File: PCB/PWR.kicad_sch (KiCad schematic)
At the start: 21 parts, among them U3 LT8610

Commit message: Fixed UART, cleaned schematic, improved LDO
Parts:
- C10, C11, C12, C13, C14, C15, C8, C9: footprint (none) -> Capacitor_SMD:C_0201_0603Metric_Pad0.64x0.40mm_HandSolder
- F2: footprint RF1180000 -> (none)
- R10, R12, R18, R7, R8, R9: footprint (none) -> Resistor_SMD:R_0603_1608Metric_Pad0.98x0.95mm_HandSolder
- renumbered PMOS to PMOS1, TVS to TVS1
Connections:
- net 3v3 renamed +3V3
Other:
- moved on the sheet: C15, LED1, R12, R7

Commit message: PCB layout v1.0
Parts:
- C10, C11, C12, C13, C14, C15, C8: footprint Capacitor_SMD:C_0201_0603Metric_Pad0.64x0.40mm_HandSolder -> Capacitor_SMD:C_0603_1608Metric_Pad1.08x0.95mm_HandSolder
- C9: footprint Capacitor_SMD:C_0201_0603Metric_Pad0.64x0.40mm_HandSolder -> Capacitor_SMD:C_0805_2012Metric_Pad1.18x1.45mm_HandSolder
- D3: value 9v zener -> BZX84B9V1; footprint (none) -> Package_TO_SOT_SMD:SOT-23
- F2: footprint (none) -> VNfootprints:polyfuse
- L2: value SPM3012T-4R7M-LR -> SPM3012T-1R5M-LR; footprint (none) -> VNfootprints:SPM3010-3020
- LED1: value Red -> LTST-C170KRKT
- PMOS1: value IRF4905 -> IRF4905STRLPBF; footprint (none) -> Package_TO_SOT_SMD:TO-263-2
- R12: value R -> 160
- TVS0: renamed from TVS1; value PTVS5V0Z1USK -> TSM24ADBZR; footprint Diode_SMD:Nexperia_DSN1608-2_1.6x0.8mm -> Package_TO_SOT_SMD:TSOT-23
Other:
- note removed: "powered via usb for flashing or only via power source? power source, no point to have separate ldo that turns on only when 24v not present and 5v present"
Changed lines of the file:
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@@
 		)
 	)
-	(text "powered via usb for flashing or only via power source?\n\npower source, no point to have separate ldo \nthat turns on only when 24v not present and 5v present\n"
-		(exclude_from_sim no)
-		(at 49.53 82.042 0)
-		(effects
-			(font
-				(size 1.27 1.27)
-			)
-		)
-	)
 	(junction
 		(at 158.75 55.88)
@@
 	)
 	(junction
+		(at 43.18 39.37)
+		(diameter 0)
+		(color 0 0 0 0)
+	)
+	(junction
 		(at 222.25 63.5)
 		(diameter 0)
@@
 	(wire
 		(pts
-			(xy 25.4 46.99) (xy 25.4 44.45)
+			(xy 146.05 76.2) (xy 146.05 73.66)
 		)
 		(stroke
@@
 	(wire
 		(pts
-			(xy 146.05 76.2) (xy 146.05 73.66)
+			(xy 25.4 44.45) (xy 26.67 44.45)
 		)
 		(stroke
@@
 	(wire
 		(pts
-			(xy 25.4 44.45) (xy 26.67 44.45)
+			(xy 177.8 63.5) (xy 175.26 63.5)
 		)
 		(stroke
@@
 	(wire
 		(pts
-			(xy 177.8 63.5) (xy 175.26 63.5)
+			(xy 166.37 60.96) (xy 167.64 60.96)
 		)
 		(stroke
@@
 	(wire
 		(pts
-			(xy 166.37 60.96) (xy 167.64 60.96)
+			(xy 222.25 58.42) (xy 222.25 63.5)
 		)
 		(stroke
@@
 	(wire
 		(pts
-			(xy 222.25 58.42) (xy 222.25 63.5)
+			(xy 228.6 45.72) (xy 228.6 48.26)
 		)
 		(stroke
@@
 	(wire
 		(pts
-			(xy 228.6 45.72) (xy 228.6 48.26)
+			(xy 25.4 44.45) (xy 25.4 39.37)
 		)
 		(stroke
@@
 	(wire
 		(pts
+			(xy 25.4 39.37) (xy 43.18 39.37)
+		)
+		(stroke
+			(width 0)
+			(type default)
+		)
+	)
+	(wire
+		(pts
 			(xy 177.8 60.96) (xy 175.26 60.96)
 		)
@@
 	(global_label "24Vin"
 		(shape input)
-		(at 25.4 46.99 270)
-		(fields_autoplaced yes)
-		(effects
-			(font
-				(size 1.27 1.27)
-			)
-			(justify right)
-		)
-		(property "Intersheetrefs" "${INTERSHEET_REFS}"
-			(at 25.4 55.2366 90)
-			(effects
-				(font
-					(size 1.27 1.27)
-				)
-				(justify right)
-				(hide yes)
-			)
-		)
-	)
-	(global_label "24Vin"
-		(shape input)
 		(at 43.18 38.1 90)
 		(fields_autoplaced yes)
@@
 		(dnp no)
 		(property "Reference" "C15"
-			(at 159.766 65.786 0)
+			(at 160.02 61.214 0)
 			(effects
 				(font
@@
 		)
 		(property "Value" "470n"
-			(at 160.528 61.468 0)
+			(at 160.782 65.786 0)
 			(effects
 				(font
@@
 			)
 		)
-		(property "Footprint" "Capacitor_SMD:C_0201_0603Metric_Pad0.64x0.40mm_HandSolder"
+		(property "Footprint" "Capacitor_SMD:C_0603_1608Metric_Pad1.08x0.95mm_HandSolder"
 			(at 153.9748 59.69 0)
 			(effects
@@
 		)
 		(property "Value" "GND"
-			(at 178.562 57.404 90)
+			(at 179.07 57.404 90)
 			(effects
 				(font
@@
 			)
 		)
-		(property "Footprint" ""
+		(property "Footprint" "VNfootprints:polyfuse"
 			(at 57.15 148.26 0)
 			(effects
@@
 			)
 		)
-		(property "Footprint" "Capacitor_SMD:C_0201_0603Metric_Pad0.64x0.40mm_HandSolder"
+		(property "Footprint" "Capacitor_SMD:C_0603_1608Metric_Pad1.08x0.95mm_HandSolder"
 			(at 175.26 59.9948 0)
 			(effects
@@
 		(dnp no)
 		(property "Reference" "C11"
-			(at 208.28 52.324 90)
+			(at 209.296 50.8 90)
 			(effects
 				(font
@@
 			)
 		)
-		(property "Footprint" "Capacitor_SMD:C_0201_0603Metric_Pad0.64x0.40mm_HandSolder"
+		(property "Footprint" "Capacitor_SMD:C_0603_1608Metric_Pad1.08x0.95mm_HandSolder"
 			(at 212.09 57.4548 0)
 			(effects
@@
 			)
 		)
-		(property "Footprint" "Capacitor_SMD:C_0201_0603Metric_Pad0.64x0.40mm_HandSolder"
+		(property "Footprint" "Capacitor_SMD:C_0805_2012Metric_Pad1.18x1.45mm_HandSolder"
 			(at 177.4952 46.99 0)
 			(effects
@@
 		(dnp no)
 		(property "Reference" "L2"
-			(at 215.9 59.69 90)
+			(at 215.646 49.784 90)
 			(effects
 				(font
@@
 			)
 		)
-		(property "Value" "SPM3012T-4R7M-LR"
-			(at 215.646 44.196 90)
+		(property "Value" "SPM3012T-1R5M-LR"
+			(at 214.884 47.498 90)
 			(effects
 				(font
@@
 			)
 		)
-		(property "Footprint" ""
+		(property "Footprint" "VNfootprints:SPM3010-3020"
 			(at 215.9 58.42 0)
 			(effects
@@
 			)
 		)
-		(property "Value" "IRF4905"
+		(property "Value" "IRF4905STRLPBF"
 			(at 46.99 45.7199 0)
 			(effects
@@
 			)
 		)
-		(property "Footprint" ""
+		(property "Footprint" "Package_TO_SOT_SMD:TO-263-2"
 			(at 45.72 41.91 0)
 			(effects
@@
 		(on_board yes)
 		(dnp no)
-		(fields_autoplaced yes)
 		(property "Reference" "R12"
-			(at 148.59 59.6899 0)
+			(at 147.32 59.69 0)
 			(effects
 				(font
@@
 			)
 		)
-		(property "Value" "R"
-			(at 148.59 62.2299 0)
+		(property "Value" "160"
+			(at 147.32 62.23 0)
 			(effects
 				(font
@@
 		(dnp no)
 		(property "Reference" "C12"
-			(at 214.376 68.834 90)
+			(at 214.884 72.898 90)
 			(effects
 				(font
@@
 		)
 		(property "Value" "4p7"
-			(at 219.456 71.374 90)
+			(at 219.71 71.882 90)
 			(effects
 				(font
@@
 			)
 		)
-		(property "Footprint" "Capacitor_SMD:C_0201_0603Metric_Pad0.64x0.40mm_HandSolder"
+		(property "Footprint" "Capacitor_SMD:C_0603_1608Metric_Pad1.08x0.95mm_HandSolder"
 			(at 214.63 70.8152 0)
 			(effects
@@
 		(dnp no)
 		(property "Reference" "C13"
-			(at 225.298 52.07 90)
+			(at 226.06 50.038 0)
 			(effects
 				(font
@@
 		)
 		(property "Value" "1u"
-			(at 231.902 52.07 90)
+			(at 230.378 50.038 0)
 			(effects
 				(font
@@
 			)
 		)
-		(property "Footprint" "Capacitor_SMD:C_0201_0603Metric_Pad0.64x0.40mm_HandSolder"
+		(property "Footprint" "Capacitor_SMD:C_0603_1608Metric_Pad1.08x0.95mm_HandSolder"
 			(at 227.6348 48.26 0)
 			(effects
@@
 		(dnp no)
 		(fields_autoplaced yes)
-		(property "Reference" "TVS1"
+		(property "Reference" "TVS0"
 			(at 71.12 57.1499 90)
 			(effects
@@
 			)
 		)
-		(property "Value" "PTVS5V0Z1USK"
+		(property "Value" "TSM24ADBZR"
 			(at 71.12 59.6899 90)
 			(effects
@@
 			)
 		)
-		(property "Footprint" "Diode_SMD:Nexperia_DSN1608-2_1.6x0.8mm"
+		(property "Footprint" "Package_TO_SOT_SMD:TSOT-23"
 			(at 64.135 58.42 0)
 			(effects
@@
 			)
 		)
-		(property "Datasheet" "https://assets.nexperia.com/documents/data-sheet/PTVS5V0Z1USK.pdf"
+		(property "Datasheet" "https://www.ti.com/lit/ds/symlink/tsm24a-q1.pdf?ts=1783418861293"
 			(at 68.58 58.42 0)
 			(effects
@@
 			)
 		)
-		(property "Description" "5V, 1200W TVS unidirectional diode, DSN1608-2"
+		(property "Description" "24V working, 38V clamp, 75nA leakage @ 24V"
 			(at 68.58 58.42 0)
 			(effects
@@
 			(project ""
 				(path "/29a68080-a031-4f05-96b8-20ecd97fb7f6/af86f007-a426-49d5-88df-f35545519537"
-					(reference "TVS1")
+					(reference "TVS0")
 					(unit 1)
 				)
@@
 		(on_board yes)
 		(dnp no)
-		(fields_autoplaced yes)
 		(property "Reference" "D3"
-			(at 30.48 38.1 0)
+			(at 27.686 45.974 0)
 			(effects
 				(font
@@
 			)
 		)
-		(property "Value" "9v zener"
-			(at 30.48 40.64 0)
+		(property "Value" "BZX84B9V1"
+			(at 27.432 48.26 0)
 			(effects
 				(font
@@
 			)
 		)
-		(property "Footprint" ""
+		(property "Footprint" "Package_TO_SOT_SMD:SOT-23"
 			(at 30.48 44.45 0)
 			(effects
@@
 		(dnp no)
 		(property "Reference" "LED1"
-			(at 139.7 68.58 90)
+			(at 134.62 69.342 90)
 			(effects
 				(font
@@
 			)
 		)
-		(property "Value" "Red"
-			(at 140.462 70.866 90)
+		(property "Value" "LTST-C170KRKT"
+			(at 129.032 72.136 90)
 			(effects
 				(font
@@
 		(dnp no)
 		(property "Reference" "C14"
-			(at 231.394 64.516 0)
+			(at 231.14 61.214 0)
 			(effects
 				(font
@@
 		)
 		(property "Value" "47u"
-			(at 231.394 67.056 0)
+			(at 231.14 63.754 0)
 			(effects
 				(font
@@
 			)
 		)
-		(property "Footprint" "Capacitor_SMD:C_0201_0603Metric_Pad0.64x0.40mm_HandSolder"
+		(property "Footprint" "Capacitor_SMD:C_0603_1608Metric_Pad1.08x0.95mm_HandSolder"
 			(at 229.5652 66.04 0)
 			(effects
@@
 			)
 		)
-		(property "Footprint" "Capacitor_SMD:C_0201_0603Metric_Pad0.64x0.40mm_HandSolder"
+		(property "Footprint" "Capacitor_SMD:C_0603_1608Metric_Pad1.08x0.95mm_HandSolder"
 			(at 190.1952 46.99 0)
 			(effects

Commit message: pcb version ready for final check
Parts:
- added NPN1: BC817-40, Package_TO_SOT_SMD:TSOT-23_HandSoldering, symbol Simulation_SPICE:NPN
- added SW1: SW_SPDT, symbol Switch:SW_SPDT
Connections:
- net +3V3: now also R12.1
- net 24Vin: now also PMOS1.3 (S), SW1.3 (C); no longer PMOS1.1 (D)
- net GND: now also NPN1.3 (E); no longer LED1.1 (K)
- net PWRSWITCH_diode: now reaches D3.2 (A), R18.1
- net PWRSWITCH_diode: now also SW1.1 (A); no longer PMOS1.2 (G)
- net at C15.2, R7.2, U3.15 (PG): now also NPN1.2 (B); no longer R12.1
- net at F2.1: now also PMOS1.1 (D); no longer PMOS1.3 (S)
- new net: LED1.1 (K), NPN1.1 (C)
- new net PWRSWITCH_gate: PMOS1.2 (G), SW1.2 (B)
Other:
- moved on the sheet: D3, F2, LED1, PMOS1, R12, R18, TVS0

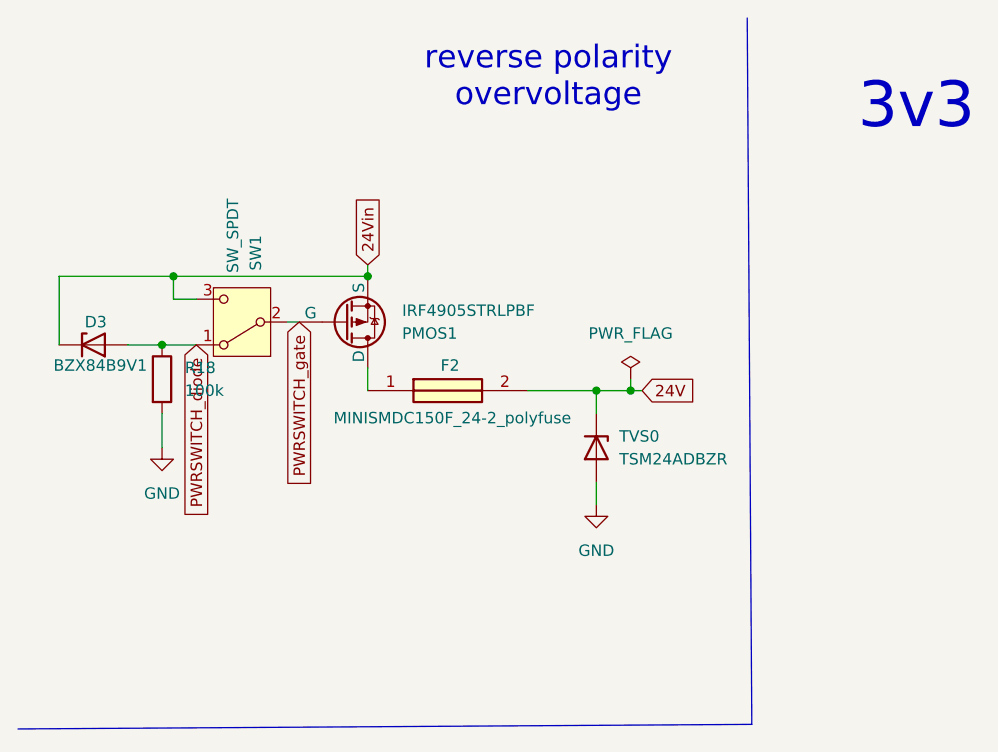
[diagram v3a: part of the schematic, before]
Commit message: [pcb] Final processing and export of production data
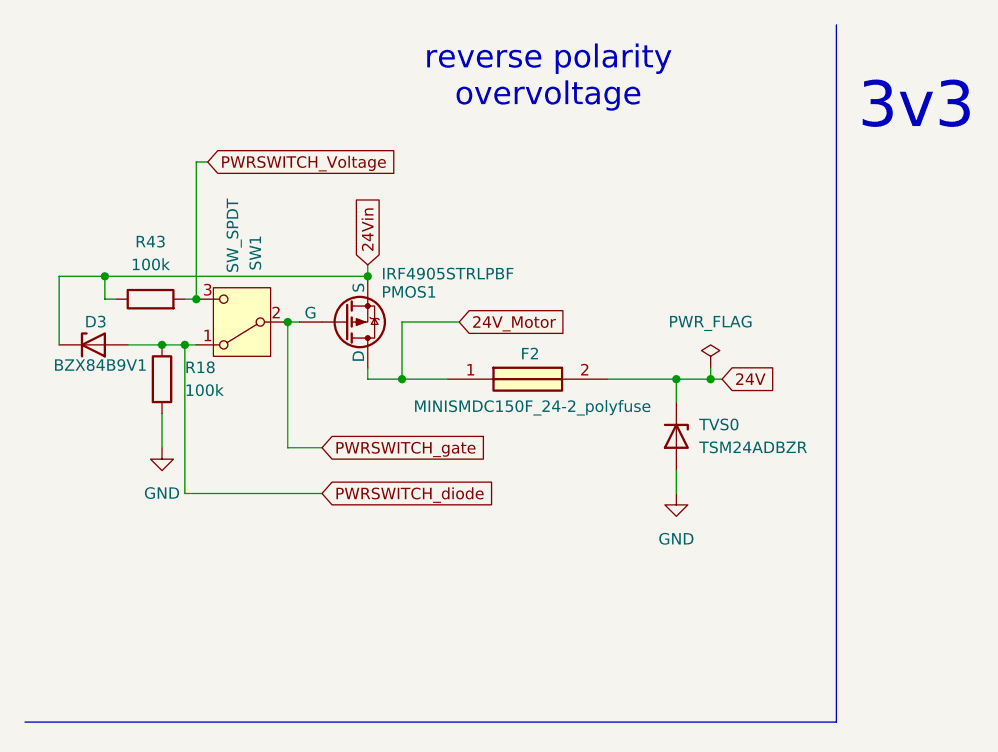
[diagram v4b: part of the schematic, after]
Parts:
- added R43: 100k, Resistor_SMD:R_0603_1608Metric_Pad0.98x0.95mm_HandSolder, symbol Device:R
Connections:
- net 24Vin: now also R43.1; no longer SW1.3 (C)
- net 24V_Motor: now reaches F2.1, PMOS1.1 (D)
- new net PWRSWITCH_Voltage: R43.2, SW1.3 (C)
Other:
- moved on the sheet: F2, TVS0
